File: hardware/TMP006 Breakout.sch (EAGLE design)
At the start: 14 parts, among them U1 TMP006

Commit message: Updates to v01: 402 -> 603 packages, added trestrict, changed trace sizes.
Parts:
- C1: device SparkFun-Capacitors:0.1UF-25V(+80/-20%)(0603) -> SparkFun-Capacitors:CAP0603-CAP
- R1, R2, R3, R4, R5: device SparkFun-Resistors:10KOHM1/10W1%(0603) -> SparkFun-Resistors:RESISTOR0603-RES
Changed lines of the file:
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@@
 <part name="SUPPLY1" library="SparkFun-Aesthetics" deviceset="VCC" device=""/>
 <part name="GND1" library="SparkFun-Aesthetics" deviceset="GND" device=""/>
-<part name="R1" library="SparkFun-Resistors" deviceset="10KOHM1/10W1%(0603)" device="" value="10k"/>
-<part name="R2" library="SparkFun-Resistors" deviceset="10KOHM1/10W1%(0603)" device="" value="10k"/>
+<part name="R1" library="SparkFun-Resistors" deviceset="RESISTOR" device="0603-RES" value="10k"/>
+<part name="R2" library="SparkFun-Resistors" deviceset="RESISTOR" device="0603-RES" value="10k"/>
 <part name="SUPPLY2" library="SparkFun-Aesthetics" deviceset="VCC" device=""/>
-<part name="R3" library="SparkFun-Resistors" deviceset="10KOHM1/10W1%(0603)" device="" value="10k"/>
-<part name="R4" library="SparkFun-Resistors" deviceset="10KOHM1/10W1%(0603)" device="" value="10k"/>
-<part name="R5" library="SparkFun-Resistors" deviceset="10KOHM1/10W1%(0603)" device="" value="10k"/>
+<part name="R3" library="SparkFun-Resistors" deviceset="RESISTOR" device="0603-RES" value="10k"/>
+<part name="R4" library="SparkFun-Resistors" deviceset="RESISTOR" device="0603-RES" value="10k"/>
+<part name="R5" library="SparkFun-Resistors" deviceset="RESISTOR" device="0603-RES" value="10k"/>
 <part name="GND2" library="SparkFun-Aesthetics" deviceset="GND" device=""/>
-<part name="C1" library="SparkFun-Capacitors" deviceset="0.1UF-25V(+80/-20%)(0603)" device="" value="0.1uF"/>
+<part name="C1" library="SparkFun-Capacitors" deviceset="CAP" device="0603-CAP" value="0.1uF"/>
 <part name="SUPPLY3" library="SparkFun-Aesthetics" deviceset="VCC" device=""/>
 <part name="GND3" library="SparkFun-Aesthetics" deviceset="GND" device=""/>

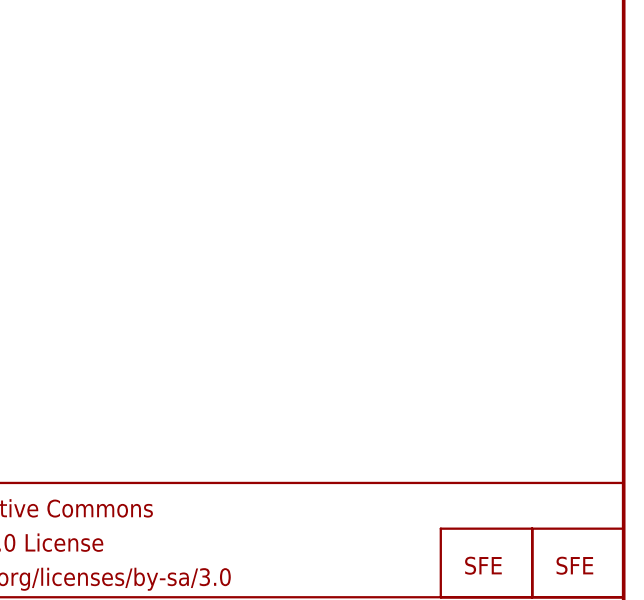
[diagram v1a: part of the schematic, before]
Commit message: Added I2C addresses on schematic, minor silk and board updates
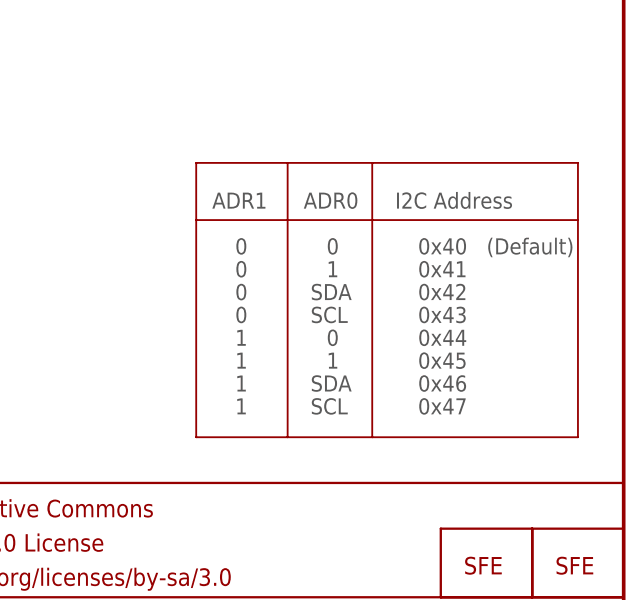
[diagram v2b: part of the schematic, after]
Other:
- note added: "(Default)"
- note added: "0"
- note added: "0x40"
- note added: "0x41"
- note added: "0x42"
- note added: "0x43"
- note added: "0x44"
- note added: "0x45"
- note added: "0x46"
- note added: "0x47"
- note added: "1"
- note added: "ADR0"
- note added: "ADR1"
- note added: "I2C Address"
- note added: "SCL"
- note added: "SDA"
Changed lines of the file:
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@@
 <text x="154.94" y="7.62" size="1.778" layer="94">Jordan McConnell</text>
 <text x="238.76" y="7.62" size="1.778" layer="94">v01</text>
+<text x="203.2" y="66.04" size="1.778" layer="97">ADR1</text>
+<text x="213.36" y="66.04" size="1.778" layer="97">ADR0</text>
+<text x="223.52" y="66.04" size="1.778" layer="97">I2C Address</text>
+<text x="205.74" y="60.96" size="1.778" layer="97">0</text>
+<text x="205.74" y="58.42" size="1.778" layer="97">0</text>
+<text x="205.74" y="55.88" size="1.778" layer="97">0</text>
+<text x="205.74" y="53.34" size="1.778" layer="97">0</text>
+<text x="215.9" y="60.96" size="1.778" layer="97">0</text>
+<text x="215.9" y="50.8" size="1.778" layer="97">0</text>
+<text x="215.9" y="58.42" size="1.778" layer="97">1</text>
+<text x="215.9" y="48.26" size="1.778" layer="97">1</text>
+<text x="205.74" y="50.8" size="1.778" layer="97">1</text>
+<text x="205.74" y="48.26" size="1.778" layer="97">1</text>
+<text x="205.74" y="45.72" size="1.778" layer="97">1</text>
+<text x="205.74" y="43.18" size="1.778" layer="97">1</text>
+<text x="214.122" y="55.88" size="1.778" layer="97">SDA</text>
+<text x="214.122" y="45.72" size="1.778" layer="97">SDA</text>
+<text x="214.122" y="53.34" size="1.778" layer="97">SCL</text>
+<text x="214.122" y="43.18" size="1.778" layer="97">SCL</text>
+<text x="226.06" y="60.96" size="1.778" layer="97">0x40</text>
+<text x="226.06" y="58.42" size="1.778" layer="97">0x41</text>
+<text x="226.06" y="55.88" size="1.778" layer="97">0x42</text>
+<text x="226.06" y="53.34" size="1.778" layer="97">0x43</text>
+<text x="226.06" y="50.8" size="1.778" layer="97">0x44</text>
+<text x="226.06" y="48.26" size="1.778" layer="97">0x45</text>
+<text x="226.06" y="45.72" size="1.778" layer="97">0x46</text>
+<text x="226.06" y="43.18" size="1.778" layer="97">0x47</text>
+<text x="233.68" y="60.96" size="1.778" layer="97">(Default)</text>
+<wire x1="201.422" y1="71.12" x2="201.422" y2="64.77" width="0.2032" layer="94"/>
+<wire x1="201.422" y1="64.77" x2="201.422" y2="40.64" width="0.2032" layer="94"/>
+<wire x1="201.422" y1="40.64" x2="211.582" y2="40.64" width="0.2032" layer="94"/>
+<wire x1="211.582" y1="40.64" x2="220.98" y2="40.64" width="0.2032" layer="94"/>
+<wire x1="220.98" y1="40.64" x2="243.84" y2="40.64" width="0.2032" layer="94"/>
+<wire x1="243.84" y1="40.64" x2="243.84" y2="64.77" width="0.2032" layer="94"/>
+<wire x1="243.84" y1="64.77" x2="243.84" y2="71.12" width="0.2032" layer="94"/>
+<wire x1="243.84" y1="71.12" x2="220.98" y2="71.12" width="0.2032" layer="94"/>
+<wire x1="220.98" y1="71.12" x2="211.582" y2="71.12" width="0.2032" layer="94"/>
+<wire x1="211.582" y1="71.12" x2="201.422" y2="71.12" width="0.2032" layer="94"/>
+<wire x1="201.422" y1="64.77" x2="243.84" y2="64.77" width="0.2032" layer="94"/>
+<wire x1="211.582" y1="71.12" x2="211.582" y2="40.64" width="0.2032" layer="94"/>
+<wire x1="220.98" y1="71.12" x2="220.98" y2="40.64" width="0.2032" layer="94"/>
 </plain>
 <instances>

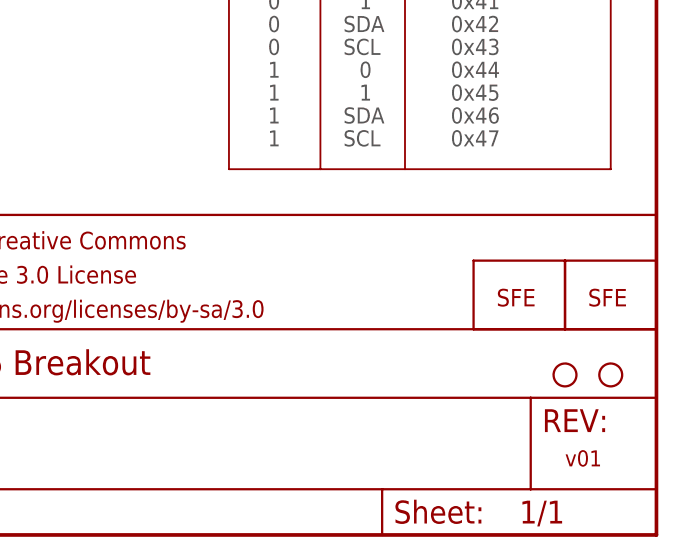
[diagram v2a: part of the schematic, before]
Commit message: Production readied
created panel
added fiducials
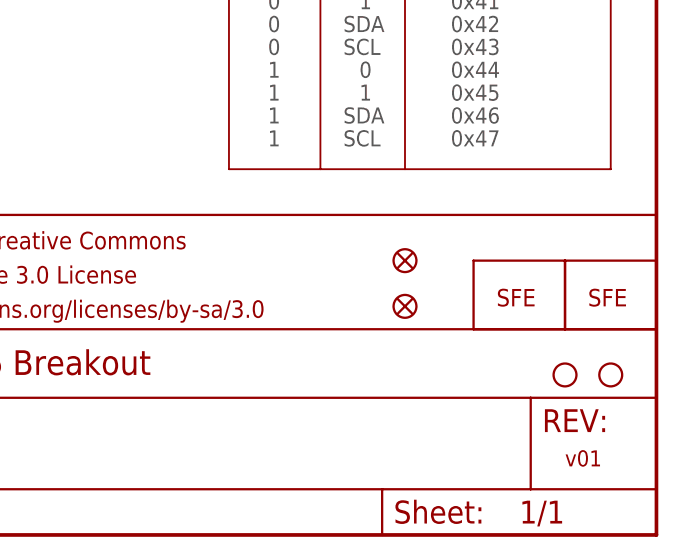
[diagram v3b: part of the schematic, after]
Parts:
- added FID1, FID2: FIDUCIALUFIDUCIAL, SparkFun-Aesthetics:FIDUCIALUFIDUCIAL
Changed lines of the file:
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@@
 <?xml version="1.0" encoding="utf-8"?>
 <!DOCTYPE eagle SYSTEM "eagle.dtd">
-<eagle version="6.2">
+<eagle version="6.4">
 <drawing>
 <settings>
@@
 <part name="STANDOFF2" library="SparkFun-Electromechanical" deviceset="STAND-OFF" device=""/>
 <part name="LOGO3" library="SparkFun-Aesthetics" deviceset="LOGO-SFE" device="NEW"/>
+<part name="FID1" library="SparkFun-Aesthetics" deviceset="FIDUCIAL" device="UFIDUCIAL"/>
+<part name="FID2" library="SparkFun-Aesthetics" deviceset="FIDUCIAL" device="UFIDUCIAL"/>
 </parts>
 <sheets>
@@
 <instance part="STANDOFF2" gate="G$1" x="238.76" y="17.78"/>
 <instance part="LOGO3" gate="G$1" x="231.14" y="25.4"/>
+<instance part="FID1" gate="G$1" x="220.98" y="30.48"/>
+<instance part="FID2" gate="G$1" x="220.98" y="25.4"/>
 </instances>
 <busses>
